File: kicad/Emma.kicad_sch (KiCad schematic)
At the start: 6 parts, among them J1 JST_GH_06P_SHLD, J2 SMA_Edge

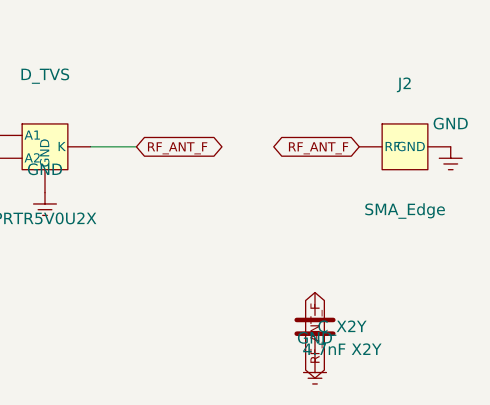
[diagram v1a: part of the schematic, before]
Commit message: Resolve Emma 49 MHz §15.203 connector violation with RP-SMA
J2 changed from a standard SMA edge jack (Amphenol 132289) to its
reverse-polarity counterpart (Amphenol 132289RP) -- identical PCB
footprint, reversed mating-pin gender -- so generic standard-SMA
antennas/cables cannot mechanically connect, satisfying 47 CFR
§15.203's "unique coupling" provision for intentional radiators.

Updates Emma.kicad_sch (lib symbol + J2 instance Value/Description),
Emma.kicad_pcb (footprint Value/Description properties, ANT silkscreen
label, ESD note), Emma.md, and the Malcolm GCS wiring/antenna-spec docs
that mirror Emma's connector on the ground station side. REFERENCES.md
and TODO.md updated from "open violation" to "resolved in design,
board re-spin pending" status.

KiCad CLI is unavailable in this environment so DRC could not be
re-run; changes are limited to text properties/silkscreen labels with
no net, pad, or geometry changes, so no DRC impact is expected.

Co-Authored-By: Claude Sonnet 4.6 <noreply@anthropic.com>
Claude-Session: https://claude.ai/code/session_014uXbK3iF9VFoBsweHtxGJL
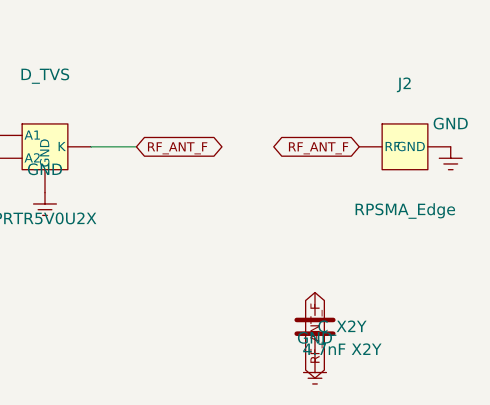
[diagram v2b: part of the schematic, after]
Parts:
- J2: value SMA_Edge -> RPSMA_Edge
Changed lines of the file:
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@@
     (property "Reference" "J2" (at 280.00 93.00 0)
       (effects (font (size 1.27 1.27))))
-    (property "Value" "SMA_Edge" (at 280.00 107.00 0)
+    (property "Value" "RPSMA_Edge" (at 280.00 107.00 0)
       (effects (font (size 1.27 1.27))))
     (property "Footprint" "Connector_Coaxial:SMA_Amphenol_132289_EdgeMount"
       (at 0 0 0) (effects (font (size 1.27 1.27)) (hide yes)))
+    (property "Description"
+      "RP-SMA edge-launch jack, 50 Ohm -- Amphenol 132289RP -- 49 MHz Part 15 15.235 antenna output, §15.203 unique coupling"
+      (at 0 0 0) (effects (font (size 1.27 1.27)) (hide yes)))
     (pin "1")

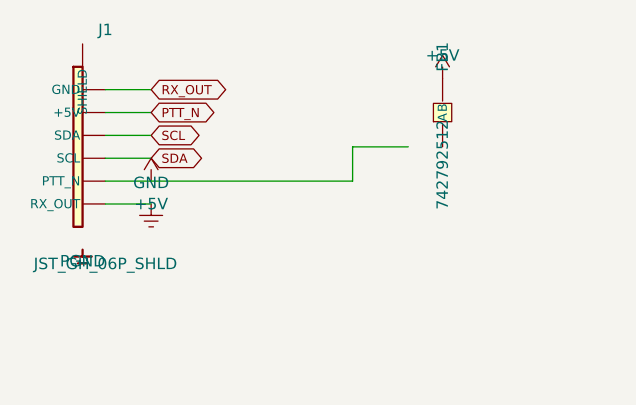
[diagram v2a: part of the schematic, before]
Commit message: Fix Emma ERC/DRC errors: schematic parser crash, J1 pin mirroring, 12 PCB shorts
Schematic (Emma.kicad_sch):
- Remove stray ;; comment that silently broke KiCad's S-expr parser,
  causing ERC to fail to load the file entirely (CLAUDE.md prohibits ;/#
  comments in KiCad files for exactly this reason).
- Fix Conn_JST_GH_06P pin Y-offset sign: J1's SHIELD/MP pin and all six
  numbered pins were mirrored relative to where their wires/power symbols
  were actually drawn, leaving the PGND bond and J1 unconnected.
- Add PWR_FLAG markers on the J1 GND/+5V/PGND nets to silence the
  power-pin-not-driven check (standard KiCad mechanism for sub-circuit
  schematics with no local power source).
- Fix FB1 wire endpoint that stopped 3.81mm short of the real pin.
ERC: 0 errors (was: file failed to load).

PCB (Emma.kicad_pcb):
- Fix 4 track segments with erroneous 2.75mm width (RF_TX, GND) that
  caused them to physically overlap nearby vias/pads despite reasonable
  centerline routing; corrected to 0.2mm/0.5mm matching established
  nets in the same area.
- Remove 3 orphaned copper stubs (TCXO_OUT, one GND stitch, one more GND
  stitch) that didn't connect to any real pad at either end and were
  shorting against unrelated nets they merely passed near.
- Reroute DDS_RF around the 49M DDS pin columns, the GND via-stitch
  fence at x=130, and neighboring components (+3V 10u, U1 ByA) instead
  of cutting through them.
- Nudge the two end vias of the x=130 GND stitching fence by 0.25mm
  (134.0/103.5 instead of 133.75/103.75) to clear PB2-P1/P2 hole
  clearance; fence interior pitch (2.5mm, 12 gaps) unchanged.
DRC: shorting_items/tracks_crossing/courtyards_overlap/hole_clearance
all at 0 (was 12/1/1/2 respectively).

Co-Authored-By: Claude Sonnet 4.6 <noreply@anthropic.com>
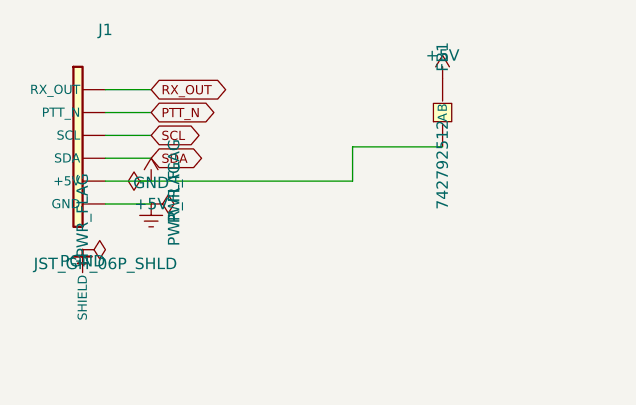
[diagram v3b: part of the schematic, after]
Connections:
- net +5V: now also FB1.1 (A), J1.2 (+5V); no longer J1.5 (PTT_N)
- net GND: now also J1.1 (GND); no longer J1.6 (RX_OUT)
- net PGND: now also J1.MP (SHIELD)
- net PTT_N: now also J1.5 (PTT_N); no longer J1.2 (+5V)
- net RX_OUT: now also J1.6 (RX_OUT); no longer J1.1 (GND)
- net SCL: now also J1.4 (SCL); no longer J1.3 (SDA)
- net SDA: now also J1.3 (SDA); no longer J1.4 (SCL)
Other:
- moved on the sheet: J1
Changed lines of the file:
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@@
     (pin "6")
     (pin "MP"))
-  ;; PGND at J1 SHIELD (MP) mounting tab — chassis ground bond for cable braid drain
   (symbol (lib_id "PGND") (at 50.00 111.43 0)
     (unit 1) (exclude_from_sim no) (in_bom no) (on_board yes) (dnp no)
     (property "Reference" "#PWR_J1_SHLD" (at 50.00 111.43 0) (effects (font (size 1.27 1.27)) (hide yes)))
     (property "Value" "PGND" (at 50.00 112.70 0) (effects (font (size 1.27 1.27))))
+    (pin "1"))
+  (symbol (lib_id "PWR_FLAG") (at 50.00 111.43 270)
+    (unit 1) (exclude_from_sim no) (in_bom no) (on_board yes) (dnp no)
+    (property "Reference" "#FLG01" (at 50.00 109.52 0) (effects (font (size 1.27 1.27)) (hide yes)))
+    (property "Value" "PWR_FLAG" (at 50.00 107.62 0) (effects (font (size 1.27 1.27))))
     (pin "1"))
   (symbol (lib_id "Ferrite_Bead") (at 90.00 96.19 90)
@@
       (effects (font (size 1.27 1.27))))
     (pin "1"))
+  (symbol (lib_id "PWR_FLAG") (at 57.62 106.35 270)
+    (unit 1) (exclude_from_sim no) (in_bom no) (on_board yes) (dnp no)
+    (property "Reference" "#FLG02" (at 57.62 109.16 0) (effects (font (size 1.27 1.27)) (hide yes)))
+    (property "Value" "PWR_FLAG" (at 60.16 106.35 0) (effects (font (size 1.27 1.27))))
+    (pin "1"))
   (symbol (lib_id "+5V") (at 57.62 103.81 0)
     (unit 1) (exclude_from_sim no) (in_bom no) (on_board yes) (dnp no)
@@
     (property "Value" "+5V" (at 57.62 106.35 0)
       (effects (font (size 1.27 1.27))))
+    (pin "1"))
+  (symbol (lib_id "PWR_FLAG") (at 57.62 103.81 90)
+    (unit 1) (exclude_from_sim no) (in_bom no) (on_board yes) (dnp no)
+    (property "Reference" "#FLG03" (at 57.62 101.27 0) (effects (font (size 1.27 1.27)) (hide yes)))
+    (property "Value" "PWR_FLAG" (at 60.16 103.81 0) (effects (font (size 1.27 1.27))))
     (pin "1"))
   (symbol (lib_id "+5V") (at 90.00 92.38 0)
@@
   (wire (pts (xy 80.00 103.81) (xy 80.00 100.00))
 )
-  (wire (pts (xy 80.00 100.00) (xy 86.19 100.00))
+  (wire (pts (xy 80.00 100.00) (xy 90.00 100.00))
 )
   (wire (pts (xy 90.00 92.38) (xy 90.00 92.38))
